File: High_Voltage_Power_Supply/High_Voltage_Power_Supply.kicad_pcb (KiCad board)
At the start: 2 copper layers, 220 x 125 mm, 110 parts, among them J1 Conn_01x02_Female, J2 Conn_01x02_Female, J3 Conn_01x02_Female, J4 Conn_01x12_Female, Q1 Q_NMOS_GDS, Q2 Q_NMOS_GDS, Q3 Q_NMOS_GDS, Q4 Q_NIGBT_GCE, U1 LT3751-TSSOP, U10 ADR3412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

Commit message: minor fix on vias not connected to anything
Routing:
- net VCC: vias 47 -> 50
- net (no net): vias 3 -> 0

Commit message: Minor bom and text change
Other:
- board text added: "200V Zener"

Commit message: Updated component list and schematic for v4
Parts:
- removed the C25 at (107.0, 76.0)
- removed the Q2 at (119.0, 88.0)
- removed U3: ZXGD3004E6, Package_TO_SOT_SMD:SOT-23-6
- D1, D2, Q1, Q4: moved to B.Cu
- Q2: renamed from Q3; moved to B.Cu
- moved Q1 27.0 mm to (120.0, 90.0), turned to 90 degrees
- moved Q4 11.5 mm to (220.0, 150.0), turned to 270 degrees
- moved Q2 7.52 mm to (120.0, 145.0), turned to 90 degrees
- moved D1 5.10 mm to (220.0, 50.0), turned to 270 degrees
- moved D2 5.10 mm to (220.0, 110.0), turned to 270 degrees
- renumbered C23 to C24, C24 to C25
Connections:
- Q1 pad 1: Drive_out -> Net-(Q1-Pad1)
- U1 pad 15: Drive_in -> Net-(Q1-Pad1)
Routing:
- net Net-(Q1-Pad1): track 0.00 -> 38.2 mm, vias 0 -> 1
- net Drive_in: track 22.3 -> 0.00 mm, vias 1 -> 0
- removed copper zone on B.Cu, net Drive_out

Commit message: updated label text
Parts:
- renumbered Q4 to Q3
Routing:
- net Net-(Q4-Pad1): track 0.00 -> 15.8 mm
- net Net-(Q3-Pad1): track 15.8 -> 0.00 mm
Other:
- board text added: "High Voltage PPT Power Supply V4 Corwin Hansen corwinh.com/git akerunakayama@gmail.com (206) 462 8204"
- board text removed: "High Voltage PPT Power Supply V3 Corwin Hansen corwinh.com/git akerunakayama@gmail.com (206) 462 8204"
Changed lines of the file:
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@@
     (zones 0)
     (modules 107)
-    (nets 60)
+    (nets 61)
   )
   (page A4)
   (layers
-    (0 F.Cu signal)
-    (31 B.Cu signal)
+    (0 F.Cu signal hide)
+    (31 B.Cu signal hide)
     (32 B.Adhes user)
     (33 F.Adhes user)
@@
   (net 58 "Net-(Q2-Pad3)")
   (net 59 "Net-(Q2-Pad1)")
+  (net 60 "Net-(Q3-Pad1)")
   (net_class Default "This is the default net class."
     (clearance 0.127)
@@
     (add_net "Net-(Q2-Pad1)")
     (add_net "Net-(Q2-Pad3)")
+    (add_net "Net-(Q3-Pad1)")
     (add_net "Net-(Q4-Pad1)")
     (add_net "Net-(R1-Pad1)")
@@
       (net 10 FIRE))
     (pad 6 smd rect (at 1.1 0.95) (size 1.06 0.65) (layers B.Cu B.Paste B.Mask)
-      (net 35 "Net-(Q4-Pad1)"))
+      (net 60 "Net-(Q3-Pad1)"))
     (pad 4 smd rect (at 1.1 -0.95) (size 1.06 0.65) (layers B.Cu B.Paste B.Mask)
-      (net 35 "Net-(Q4-Pad1)"))
+      (net 60 "Net-(Q3-Pad1)"))
     (pad 3 smd rect (at -1.1 -0.95) (size 1.06 0.65) (layers B.Cu B.Paste B.Mask)
       (net 1 GND))
@@
     (descr "TO-247-3, Vertical, RM 5.45mm, see https://toshiba.semicon-storage.com/us/product/mosfet/to-247-4l.html")
     (tags "TO-247-3 Vertical RM 5.45mm")
-    (fp_text reference Q4 (at 5.45 3.45 270) (layer B.SilkS)
+    (fp_text reference Q3 (at 5.45 3.45 270) (layer B.SilkS)
       (effects (font (size 1 1) (thickness 0.15)) (justify mirror))
     )
@@
       (net 56 "Net-(D12-Pad1)"))
     (pad 1 thru_hole rect (at 0 0 270) (size 2.5 4.5) (drill 1.5) (layers *.Cu *.Mask)
-      (net 35 "Net-(Q4-Pad1)"))
+      (net 60 "Net-(Q3-Pad1)"))
     (model ${KISYS3DMOD}/Package_TO_SOT_THT.3dshapes/TO-247-3_Vertical.wrl
       (at (xyz 0 0 0))
@@
     (effects (font (size 1 1) (thickness 0.15)))
   )
-  (gr_text "High Voltage PPT Power Supply V3\nCorwin Hansen\ncorwinh.com/git\nakerunakayama@gmail.com\n(206) 462 8204" (at 60.4 83.7 90) (layer B.SilkS)
+  (gr_text "High Voltage PPT Power Supply V4\nCorwin Hansen\ncorwinh.com/git\nakerunakayama@gmail.com\n(206) 462 8204" (at 60.4 83.7 90) (layer B.SilkS)
     (effects (font (size 1.5 1.5) (thickness 0.3)) (justify mirror))
   )

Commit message: Component updates for new version
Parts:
- removed C16, C17: 0.1uF, Capacitor_SMD:C_1206_3216Metric
- removed the C26 at (85.1, 88.0)
- removed the C27 at (89.2, 75.3)
- removed C32, C33: 10uF, Capacitor_SMD:C_1206_3216Metric
- removed C6, C7, C8: 1000uF, Capacitor_THT:CP_Radial_D18.0mm_P7.50mm
- removed D10, D11, D12, D13, D14, D15, D4, D5, D6, D7, D8, D9: CMZ5956B, Diode_SMD:D_SMA
- removed the H4 at (100.0, 159.0)
- removed H5: MountingHole_Pad, MountingHole:MountingHole_3.2mm_M3
- removed R27: 4.7k, Resistor_SMD:R_1206_3216Metric
- removed U10: ADR3412, Package_TO_SOT_SMD:SOT-23-6
- removed U8: LM7805, Package_TO_SOT_SMD:SOT-223-3_TabPin2
- removed U9: LMV331, Package_TO_SOT_SMD:SOT-353_SC-70-5
- C1, C19, C2, C20, C21, C22, C3, C4, C5, L1: moved to B.Cu
- H3: footprint MountingHole:MountingHole_3.2mm_M3_Pad_Via -> MountingHole:MountingHole_3.2mm_M3
- moved H4 87.4 mm to (150.0, 135.0)
- moved Q3 60.5 mm to (167.5, 120.0)
- moved C18 59.6 mm to (132.5, 105.0)
- moved TR3 56.5 mm to (110.0, 117.5)
- moved C28 55.9 mm to (157.0, 134.0)
- moved U4 55.9 mm to (161.0, 134.0)
- moved D2 54.0 mm to (167.5, 97.5)
- moved TR1 53.5 mm to (110.0, 70.0)
- moved TR2 53.5 mm to (144.0, 70.0)
- moved D1 52.5 mm to (167.5, 50.0)
- moved J3 52.2 mm to (180.0, 130.0)
- moved C34 51.1 mm to (180.0, 64.5)
- moved J2 51.0 mm to (180.0, 80.0)
- moved H3 50.0 mm to (150.0, 45.0)
- moved R6 41.6 mm to (163.5, 47.5)
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- renumbered C24 to C26, C25 to C27, H6 to H4
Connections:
- H3 pad 1: GND -> (no net)
- J4 pad 5: +5VD -> VCC
- J4 pad 7: Charged -> +5VD
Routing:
- net VCC: track 415.1 -> 0.00 mm, vias 50 -> 0
- net FIRE: track 247.4 -> 0.00 mm, vias 1 -> 0
- net +5VD: track 159.2 -> 0.00 mm, vias 13 -> 0
- net CHARGE: track 117.1 -> 0.00 mm, vias 2 -> 0
- net ~FAULT~: track 116.3 -> 0.00 mm, vias 2 -> 0
- net Net-(R6-Pad2): track 104.4 -> 0.00 mm
- net Charged: track 102.7 -> 0.00 mm, vias 2 -> 0
- net Net-(C18-Pad1): track 91.0 -> 0.00 mm
- net CHARGE_IGN: track 78.0 -> 0.00 mm, vias 2 -> 0
- net ~FAULT_IGN~: track 73.0 -> 0.00 mm, vias 2 -> 0
- net GND: track 71.0 -> 0.00 mm, vias 254 -> 0
- net Vtrans: track 69.1 -> 0.00 mm, vias 26 -> 0
- net Net-(Q1-Pad1): track 38.2 -> 0.00 mm, vias 1 -> 0
- net Net-(Q2-Pad1): track 26.7 -> 0.00 mm, vias 3 -> 0
- net Net-(Q1-Pad3): track 25.9 -> 0.00 mm
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- removed copper zone on B.Cu, net +5VA
- removed copper zone on F.Cu, net +5VD
- removed copper zone on F.Cu, net /Transformer/in-
- removed copper zone on B.Cu, net /Transformer/out+
- removed copper zone on F.Cu, net /Transformer/out+
- removed copper zone on B.Cu, net Charged
- removed copper zone on B.Cu, net GND
- removed copper zone on F.Cu, net GND
- removed copper zone on F.Cu, net Net-(C14-Pad1)
- removed copper zone on F.Cu, net Net-(C15-Pad1)
- removed copper zone on F.Cu, net Net-(C15-Pad2)
- removed copper zone on B.Cu, net Net-(C17-Pad1)
- removed copper zone on B.Cu, net Net-(C18-Pad1)
- removed copper zone on B.Cu, net Net-(C34-Pad1)
- removed copper zone on B.Cu, net Net-(C35-Pad1)
- removed copper zone on B.Cu, net Net-(C36-Pad1)
- removed copper zone on F.Cu, net Net-(D10-Pad1)
- removed copper zone on F.Cu, net Net-(D10-Pad2)
- removed copper zone on F.Cu, net Net-(D12-Pad2)
- removed copper zone on F.Cu, net Net-(D2-Pad2)
- removed copper zone on F.Cu, net Net-(D3-Pad1)
- removed copper zone on F.Cu, net Net-(J3-Pad1)
- removed copper zone on F.Cu, net Net-(Q1-Pad3)
- removed copper zone on F.Cu, net Net-(Q2-Pad3)
- removed copper zone on B.Cu, net VCC
- removed copper zone on F.Cu, net VCC
- removed copper zone on B.Cu, net Vtrans
- removed copper zone on F.Cu, net Vtrans
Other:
- board size 220 x 125 mm -> 170 x 100 mm
- board text removed: "CGD"

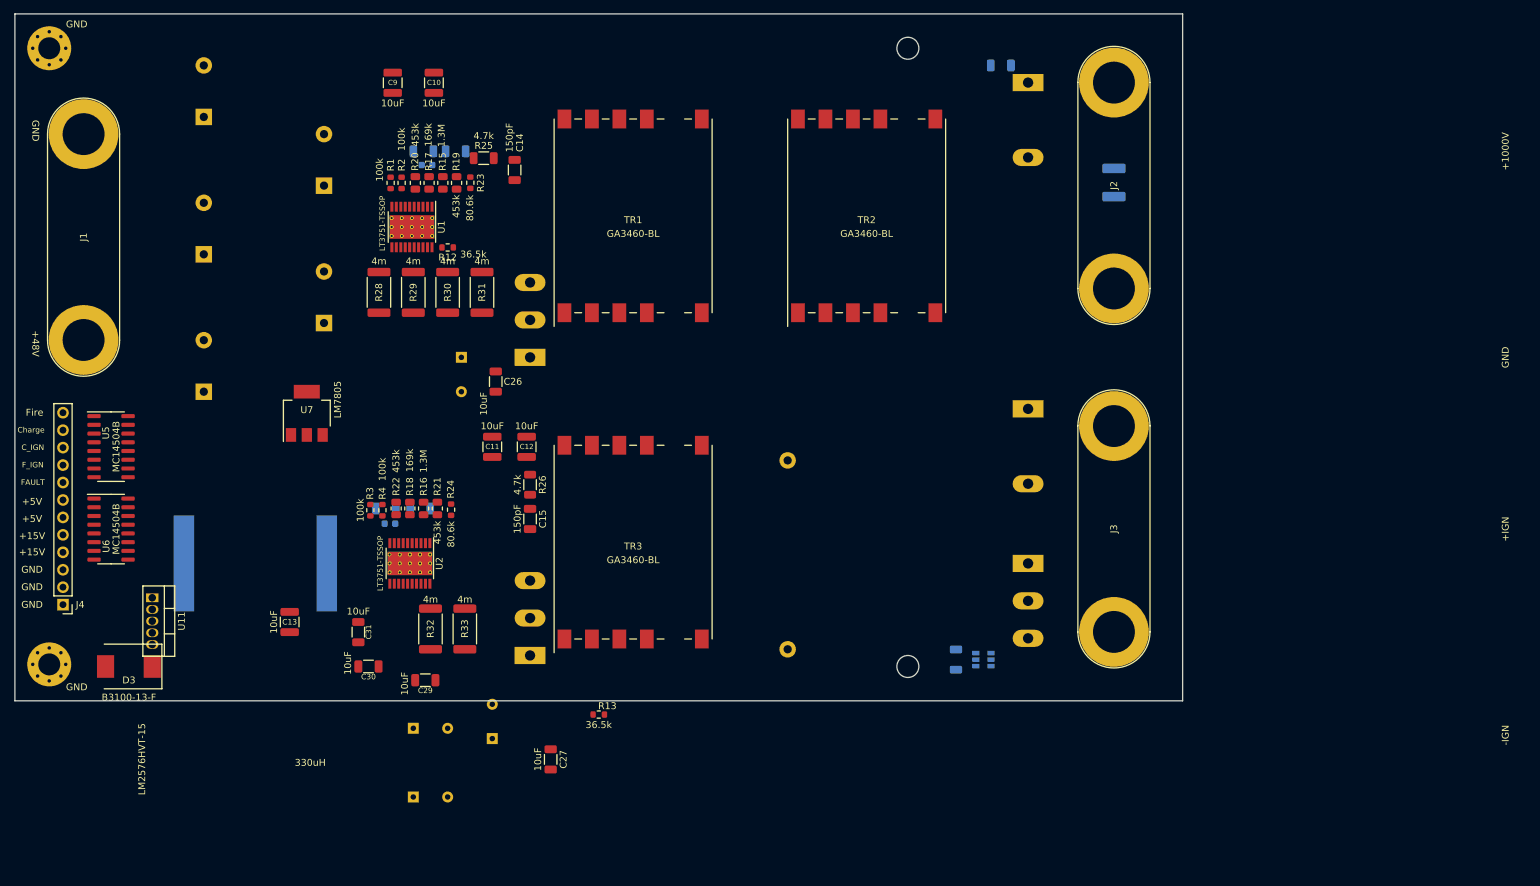
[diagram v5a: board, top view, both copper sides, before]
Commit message: updated components to match new requirements from experiments
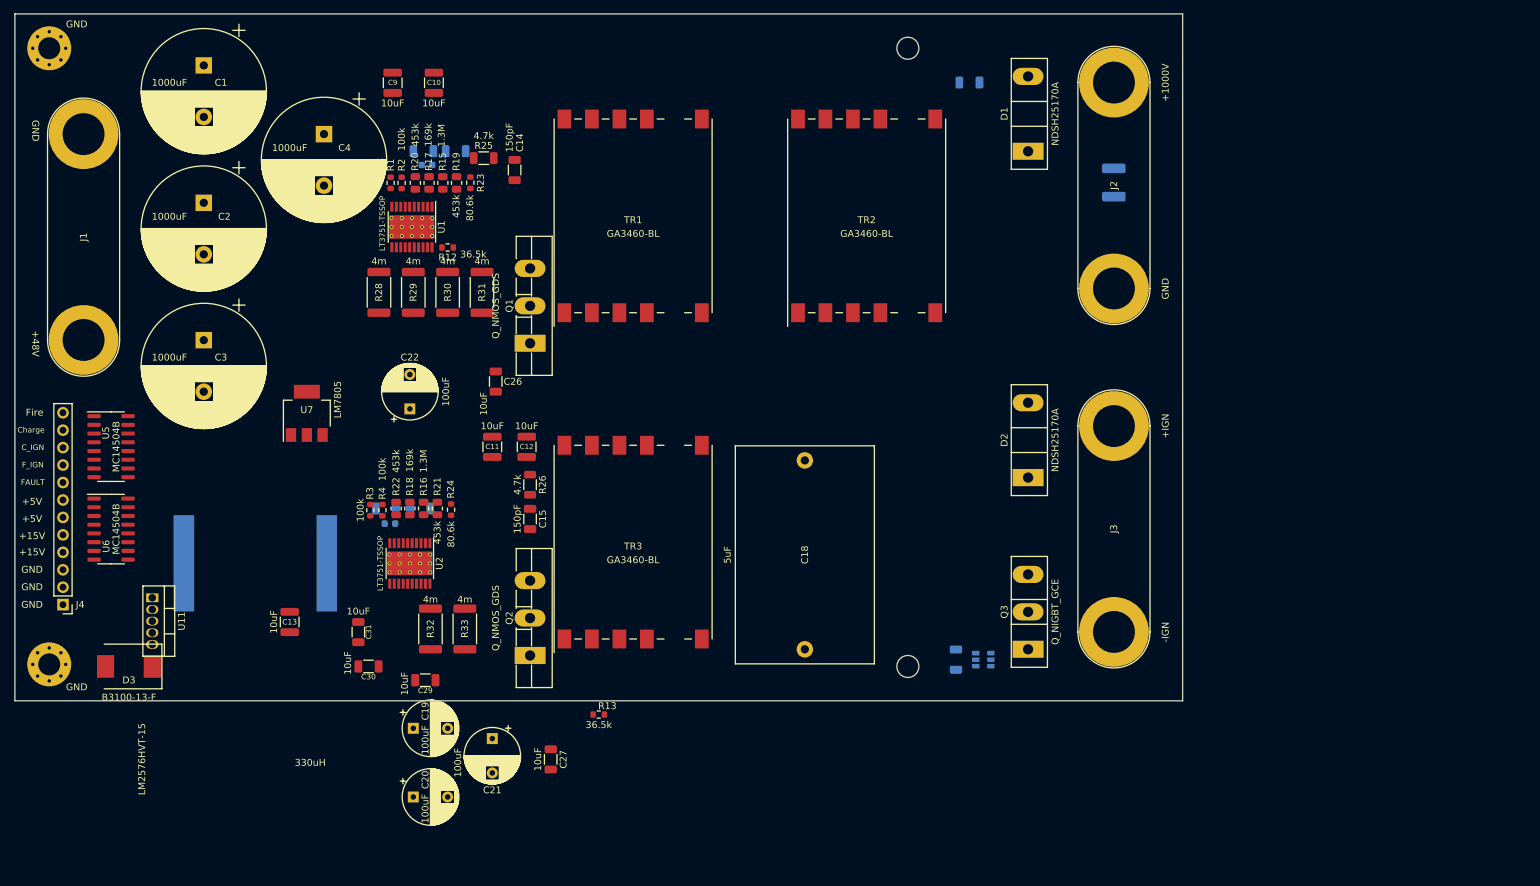
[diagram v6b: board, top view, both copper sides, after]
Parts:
- removed C5: 1000uF, Capacitor_THT:CP_Radial_D18.0mm_P7.50mm
- C1, C18, C19, C2, C20, C21, C22, C3, C4, D1, D2, Q1, Q2, Q3: moved to F.Cu
- moved C4 41.4 mm to (65.0, 57.5), turned to 270 degrees
- moved C3 28.5 mm to (47.5, 87.5), turned to 270 degrees
- moved Q3 12.5 mm to (167.5, 132.5), turned to 90 degrees
- moved C22 10.6 mm to (77.5, 97.5), turned to 90 degrees
- moved D1 10.0 mm to (167.5, 60.0), turned to 90 degrees
- moved D2 10.0 mm to (167.5, 107.5), turned to 90 degrees
- moved C1 7.50 mm to (47.5, 47.5), turned to 270 degrees
- moved C2 7.50 mm to (47.5, 67.5), turned to 270 degrees
- moved R6 5.21 mm to (159.0, 50.0)
- moved C18 2.50 mm to (135.0, 105.0)
- moved Q1 2.05 mm to (95.0, 88.0)
- turned C21 to 270 degrees

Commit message: finished pcb v4 layout. Added cad for heatsink.
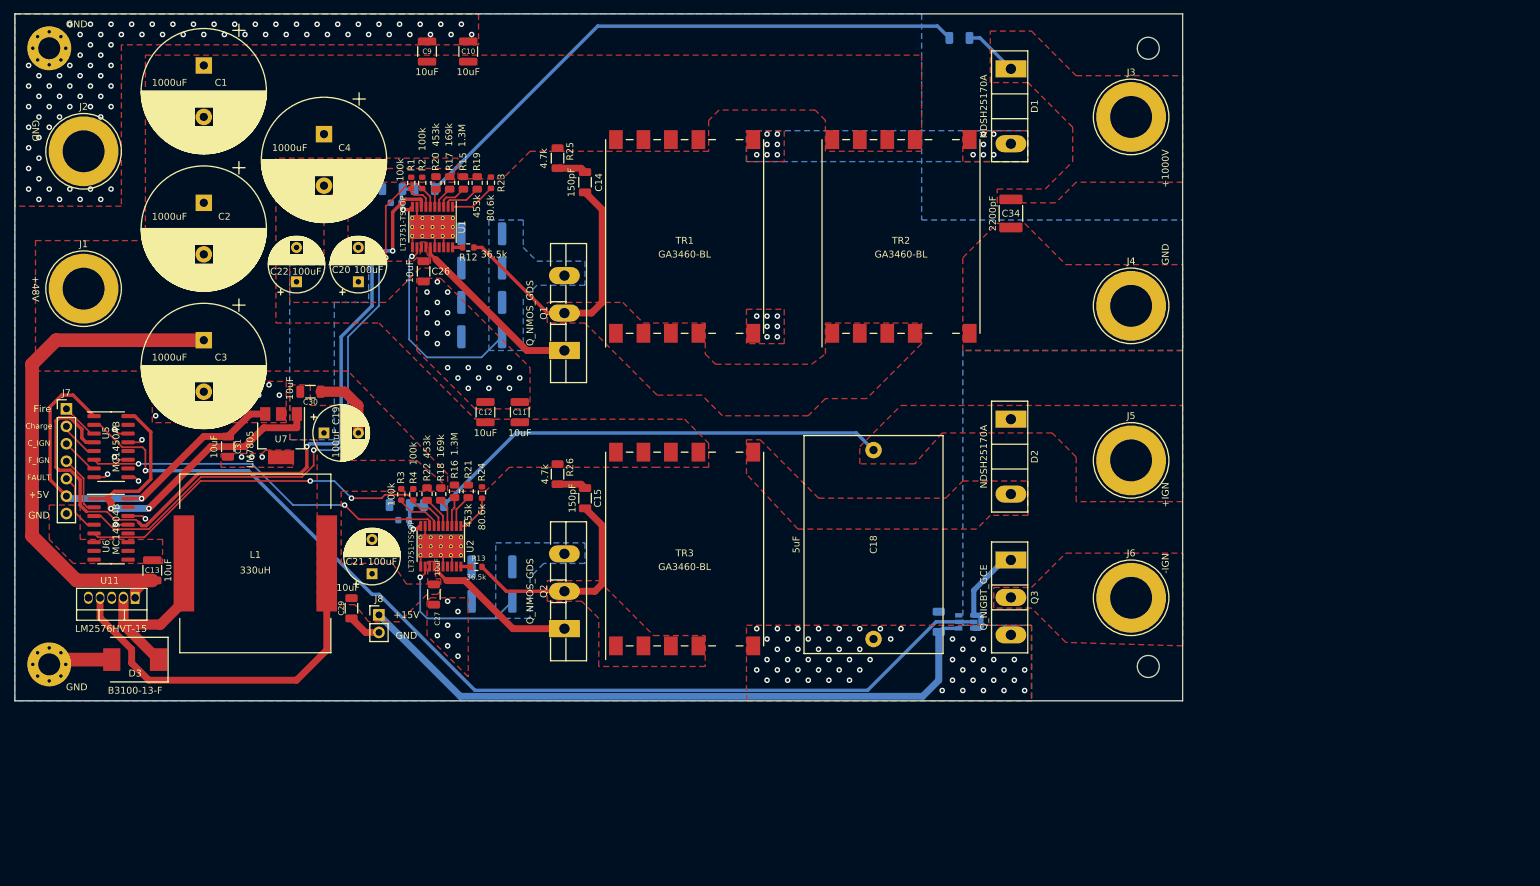
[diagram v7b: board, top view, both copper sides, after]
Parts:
- added J5: Conn_01x01_Male, Connector:Banana_Jack_1Pin, F.Cu at (182.5, 105.0)
- added J6: Conn_01x01_Male, Connector:Banana_Jack_1Pin, F.Cu at (182.5, 125.0)
- added J7: Conn_01x07_Female, Connector_PinHeader_2.54mm:PinHeader_1x07_P2.54mm_Vertical, F.Cu at (27.5, 97.5)
- added J8: Conn_01x02_Female, Connector_PinHeader_2.54mm:PinHeader_1x02_P2.54mm_Vertical, F.Cu at (73.0, 127.5)
- C34, L1: moved to F.Cu
- J1, J2, J3: value Conn_01x02_Female -> Conn_01x01_Male; footprint Connector:Banana_Jack_2Pin -> Connector:Banana_Jack_1Pin
- J4: value Conn_01x12_Female -> Conn_01x01_Male; footprint Connector_PinHeader_2.54mm:PinHeader_1x12_P2.54mm_Vertical -> Connector:Banana_Jack_1Pin
- R28, R29, R30, R31, R32, R33: moved to B.Cu
- moved J4 161.5 mm to (182.5, 82.5), turned to 0 degrees
- moved J2 151.3 mm to (30.0, 60.0), turned to 0 degrees
- moved C20 75.4 mm to (70.0, 79.0), turned to 90 degrees
- moved J3 75.0 mm to (182.5, 55.0), turned to 0 degrees
- moved C19 44.9 mm to (65.0, 101.0)
- moved C30 40.9 mm to (63.0, 95.0)
- moved H3 35.0 mm to (185.0, 45.0)
- moved H4 35.0 mm to (185.0, 135.0)
- moved C31 33.0 mm to (51.0, 103.0)
- moved C21 29.7 mm to (72.0, 121.5), turned to 90 degrees
- moved C27 29.4 mm to (81.0, 124.5)
- moved R13 27.9 mm to (87.2, 120.5)
- moved C22 24.8 mm to (61.0, 79.0)
- moved J1 22.5 mm to (30.0, 80.0), turned to 0 degrees
- moved C13 21.4 mm to (40.0, 121.0), turned to 90 degrees
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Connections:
- J1 pad 1: GND -> Vtrans
- J3 pad 1: Net-(J3-Pad1) -> Net-(C34-Pad1)
- Q3 pad 2: Net-(J3-Pad1) -> Net-(J6-Pad1)
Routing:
- net VCC: track 0.00 -> 208.9 mm, vias 0 -> 2
- net FIRE: track 0.00 -> 150.1 mm, vias 0 -> 1
- net CHARGE: track 0.00 -> 111.7 mm, vias 0 -> 2
- net ~FAULT~: track 0.00 -> 90.7 mm, vias 0 -> 2
- net Net-(R6-Pad2): track 0.00 -> 85.5 mm
- net Vtrans: track 0.00 -> 75.8 mm
- net Net-(C18-Pad1): track 0.00 -> 67.9 mm
- net +5VD: track 0.00 -> 58.5 mm, vias 0 -> 1
- net ~FAULT_IGN~: track 0.00 -> 58.0 mm, vias 0 -> 2
- net GND: track 0.00 -> 54.2 mm, vias 0 -> 206
- net CHARGE_IGN: track 0.00 -> 53.3 mm, vias 0 -> 2
- net /Transformer/in-: track 0.00 -> 40.3 mm
- net Net-(C15-Pad2): track 0.00 -> 31.5 mm
- net Net-(Q1-Pad3): track 0.00 -> 29.9 mm, vias 0 -> 1
- net Net-(D3-Pad1): track 0.00 -> 26.8 mm
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- added copper zone on F.Cu, net /Transformer/in-
- added copper zone on B.Cu, net /Transformer/out+
- added copper zone on F.Cu, net /Transformer/out+
- added copper zone on B.Cu, net GND
- added copper zone on F.Cu, net GND
- added copper zone on F.Cu, net Net-(C15-Pad2)
- added copper zone on F.Cu, net Net-(C18-Pad1)
- added copper zone on F.Cu, net Net-(C34-Pad1)
- added copper zone on F.Cu, net Net-(D2-Pad2)
- added copper zone on F.Cu, net Net-(J6-Pad1)
- added copper zone on B.Cu, net Net-(Q1-Pad3)
- added copper zone on B.Cu, net Net-(Q2-Pad3)
- added copper zone on B.Cu, net VCC
- added copper zone on F.Cu, net VCC
- added copper zone on F.Cu, net Vtrans
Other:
- net class High Voltage: clearance 5.588 -> 2.5
- net class High Voltage Low Clearence: clearance 1.27 -> 1.5
- net class Mid Voltage: clearance 1.27 -> 1
- net class Mid Voltage Low Clearence: clearance 0.127 -> 0.5

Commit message: minor layout update
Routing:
- net GND: vias 206 -> 185
